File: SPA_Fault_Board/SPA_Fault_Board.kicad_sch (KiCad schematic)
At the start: 52 parts, among them Q1 2N3905, SW1 SW_SPST, T1 Transformer_1P_2S, U1 LM7805

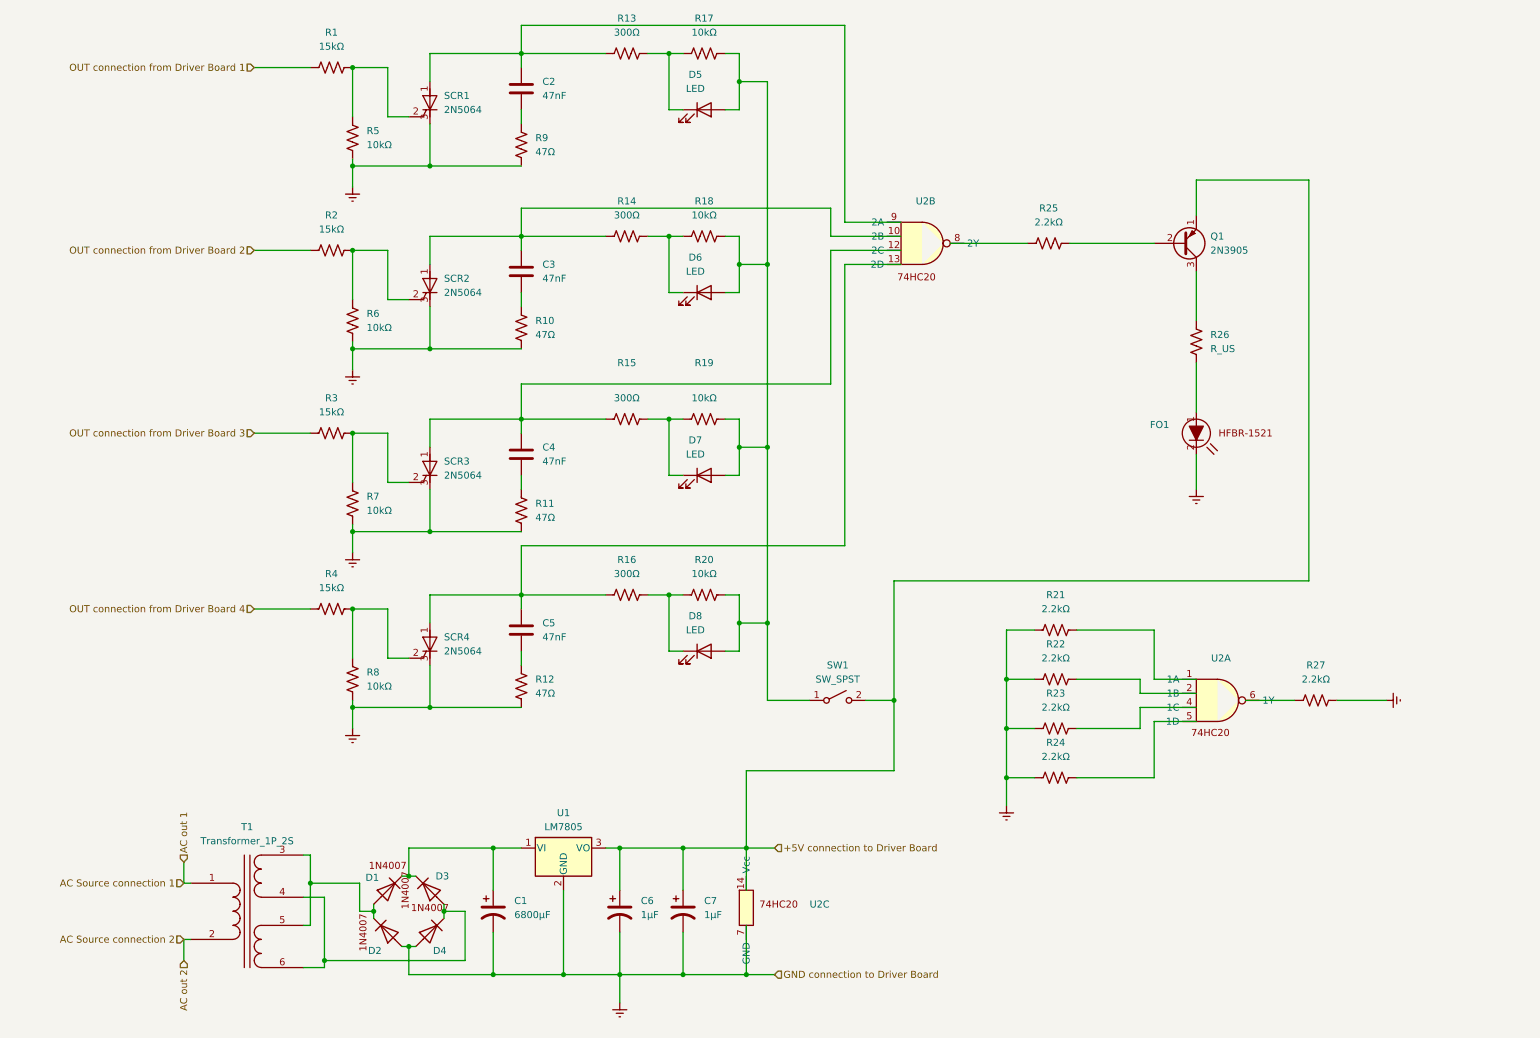
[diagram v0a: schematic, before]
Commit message: Added SPA to complete schematic
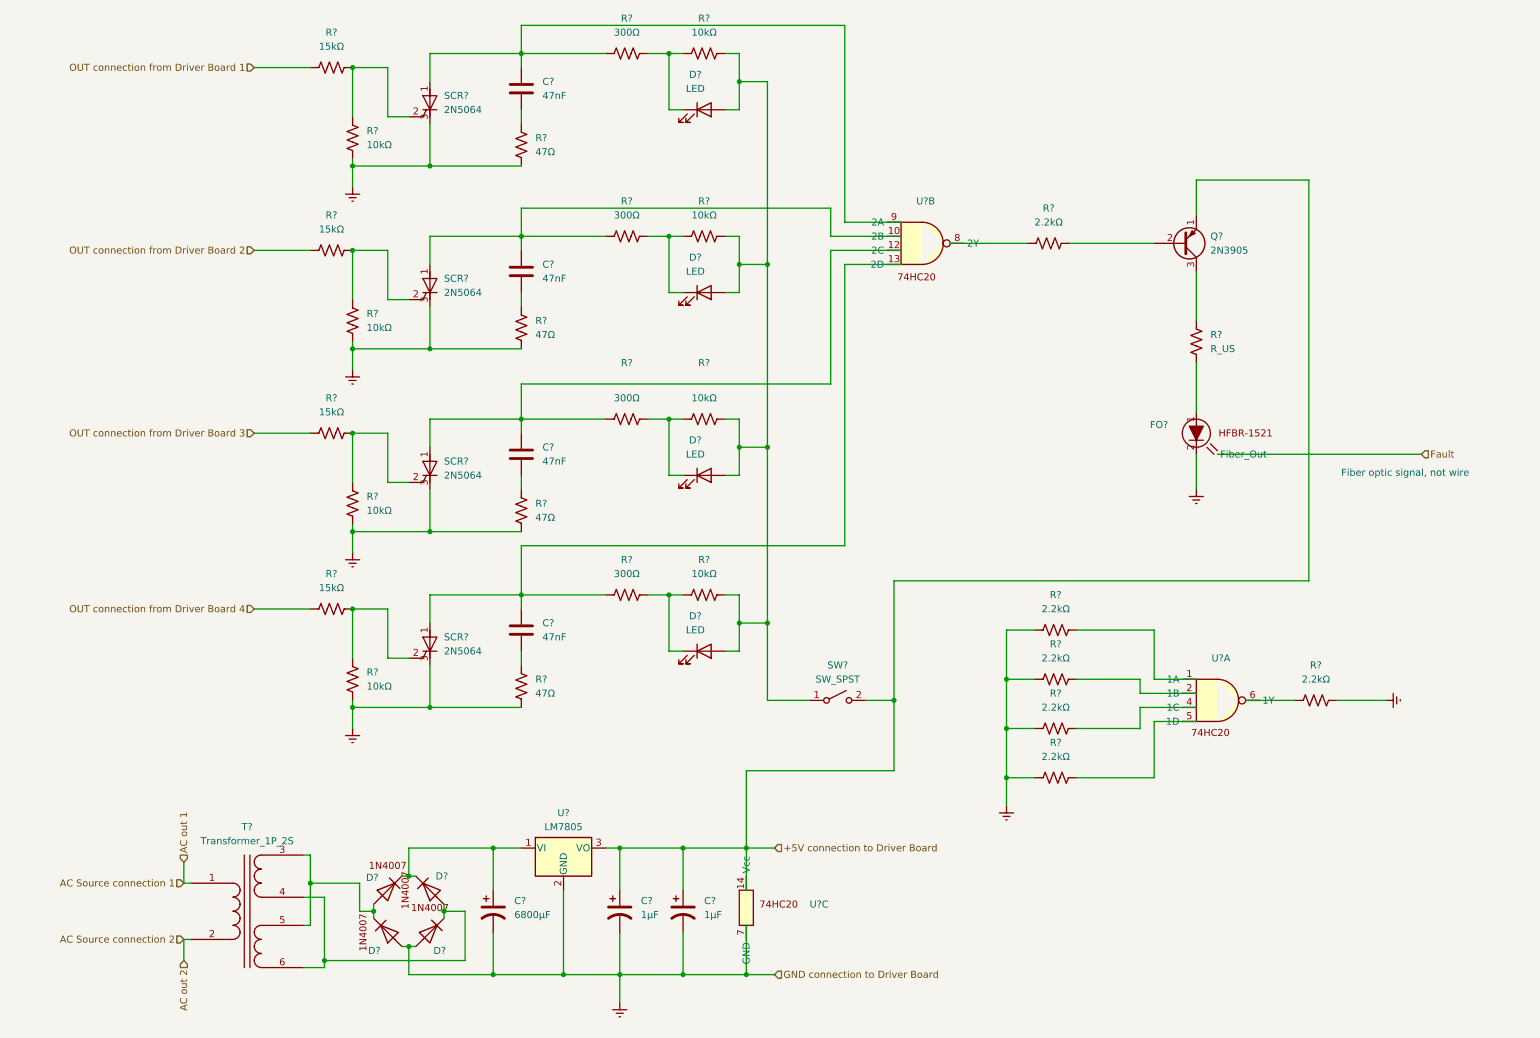
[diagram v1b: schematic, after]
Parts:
- renumbered C6 to C?, C7 to C?, C5 to C?, C2 to C?, C4 to C?, C1 to C?, C3 to C?, D2 to D?, D8 to D?, D5 to D?, D3 to D?, D6 to D?, D7 to D?, D4 to D?, D1 to D?, FO1 to FO?, Q1 to Q?, R2 to R?, R19 to R?, R27 to R?, R8 to R?, R22 to R?, R23 to R?, R9 to R?, R11 to R?, R4 to R?, R20 to R?, R13 to R?, R15 to R?, R17 to R?, R16 to R?, R18 to R?, R1 to R?, R6 to R?, R25 to R?, R3 to R?, R5 to R?, R12 to R?, R21 to R?, R7 to R?, R10 to R?, R26 to R?, R14 to R?, R24 to R?, SCR4 to SCR?, SCR2 to SCR?, SCR1 to SCR?, SCR3 to SCR?, SW1 to SW?, T1 to T?, U2 to U?, U1 to U?
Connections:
- new net Fault: FO?. (Fiber_Out)
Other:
- note added: "Fiber optic signal, not wire"
